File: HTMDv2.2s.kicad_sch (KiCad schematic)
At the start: 94 parts, among them IC1 TJA1441AT_0Z, IC2 A3921KLPTR-T, IC3 TMP275AQDGKRQ1, J1 Conn_01x04, J10 Conn_01x02, J11 Conn_01x02, J2 Conn_01x04, J3 Conn_01x06, J4 Conn_01x01, J5 Conn_01x01_Pin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

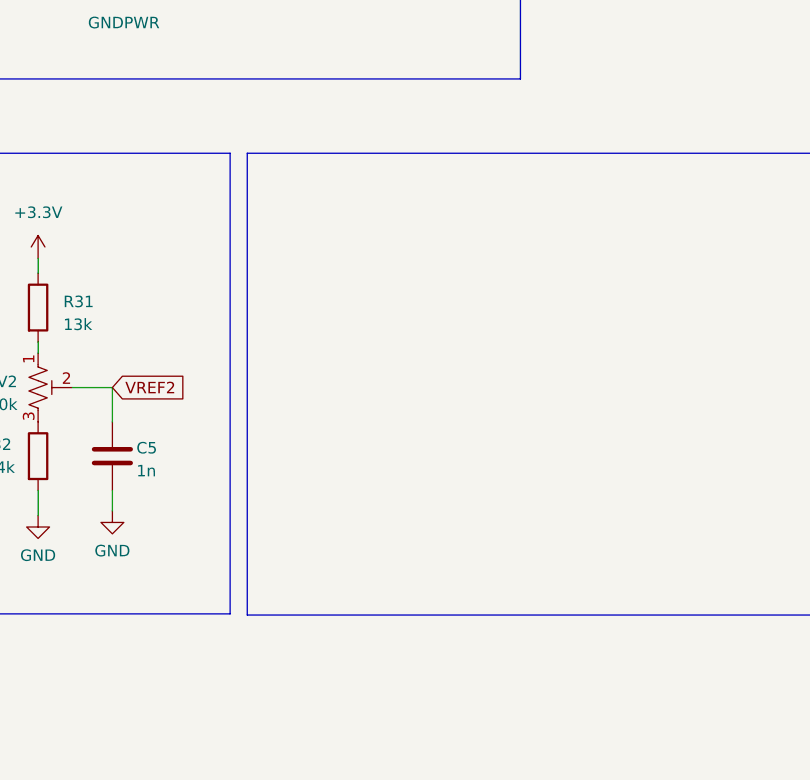
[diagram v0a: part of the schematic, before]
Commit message: Update HTMDv2.2s.kicad_sch
add LEDs
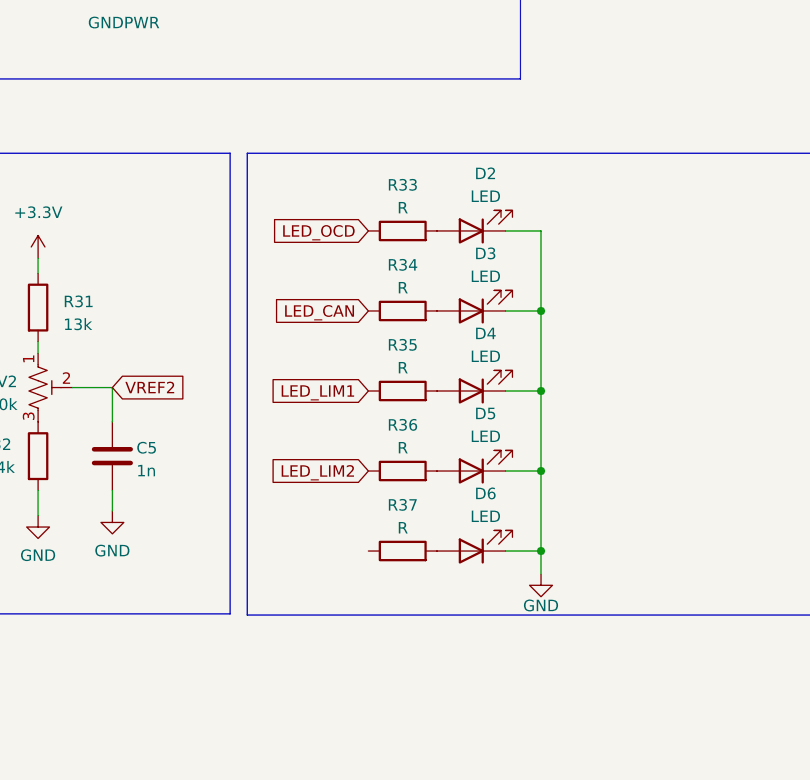
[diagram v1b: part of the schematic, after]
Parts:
- added D2, D3, D4, D5, D6: LED, LED_SMD:LED_0603_1608Metric_Pad1.05x0.95mm_HandSolder, symbol Device:LED
- added R33, R34, R35, R36, R37: R, Resistor_SMD:R_0603_1608Metric_Pad0.98x0.95mm_HandSolder, symbol Device:R
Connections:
- net GND: now also D2.1 (K), D3.1 (K), D4.1 (K), D5.1 (K), D6.1 (K)
- net LED_CAN: now also R34.1
- net LED_LIM1: now also R35.1
- net LED_LIM2: now also R36.1
- net LED_OCD: now also R33.1
- new net: D4.2 (A), R35.2
- new net: D3.2 (A), R34.2
- new net: D5.2 (A), R36.2
- new net: D6.2 (A), R37.2
- new net: D2.2 (A), R33.2

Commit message: update
change footprints
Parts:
- C7: footprint Capacitor_SMD:C_0402_1005Metric_Pad0.74x0.62mm_HandSolder -> Capacitor_SMD:C_0603_1608Metric_Pad1.08x0.95mm_HandSolder
- J6: footprint Connector_PinHeader_2.54mm:PinHeader_1x02_P2.54mm_Horizontal -> TestPoint:TestPoint_2Pads_Pitch2.54mm_Drill0.8mm
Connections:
- net SWCLK: now also J9.1 (Pin_1); no longer J9.3 (Pin_3)
- net SWDIO: now also J9.3 (Pin_3); no longer J9.1 (Pin_1)
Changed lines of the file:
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@@
     )
   )
-  (global_label "SWCLK" (shape input) (at 381 40.259 0) (fields_autoplaced)
-    (effects (font (size 1.27 1.27)) (justify left))
-    (property "Intersheetrefs" "${INTERSHEET_REFS}" (at 390.2142 40.259 0)
+  (global_label "SWCLK" (shape input) (at 381 45.339 0) (fields_autoplaced)
+    (effects (font (size 1.27 1.27)) (justify left))
+    (property "Intersheetrefs" "${INTERSHEET_REFS}" (at 390.2142 45.339 0)
       (effects (font (size 1.27 1.27)) (justify left) hide)
     )
@@
     )
   )
-  (global_label "SWDIO" (shape input) (at 381 45.339 0) (fields_autoplaced)
-    (effects (font (size 1.27 1.27)) (justify left))
-    (property "Intersheetrefs" "${INTERSHEET_REFS}" (at 389.8514 45.339 0)
+  (global_label "SWDIO" (shape input) (at 381 40.259 0) (fields_autoplaced)
+    (effects (font (size 1.27 1.27)) (justify left))
+    (property "Intersheetrefs" "${INTERSHEET_REFS}" (at 389.8514 40.259 0)
       (effects (font (size 1.27 1.27)) (justify left) hide)
     )
@@
       (effects (font (size 1.27 1.27)))
     )
-    (property "Footprint" "Capacitor_SMD:C_0402_1005Metric_Pad0.74x0.62mm_HandSolder" (at 216.027 240.0808 0)
+    (property "Footprint" "Capacitor_SMD:C_0603_1608Metric_Pad1.08x0.95mm_HandSolder" (at 216.027 240.0808 0)
       (effects (font (size 1.27 1.27)) hide)
     )
@@
       (effects (font (size 1.27 1.27)))
     )
-    (property "Footprint" "Connector_PinHeader_2.54mm:PinHeader_1x02_P2.54mm_Horizontal" (at 365.633 62.103 0)
-      (effects (font (size 1.27 1.27)) hide)
-    )
+    (property "Footprint" "TestPoint:TestPoint_2Pads_Pitch2.54mm_Drill0.8mm" (at 365.633 62.103 0)
+      (effects (font (size 1.27 1.27)) hide)
+    )

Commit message: update
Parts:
- added R38: 20k, Resistor_SMD:R_0603_1608Metric_Pad0.98x0.95mm_HandSolder, symbol Device:R
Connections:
- net GND: now also R38.2; no longer U2.46 (PB8)
- new net: R38.1, U2.46 (PB8)
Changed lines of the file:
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@@
     (stroke (width 0) (type default))
   )
-  (wire (pts (xy 64.389 199.263) (xy 64.389 180.975))
+  (wire (pts (xy 64.389 199.263) (xy 64.389 195.072))
     (stroke (width 0) (type default))
   )
@@
     (stroke (width 0) (type default))
   )
+  (wire (pts (xy 64.389 187.452) (xy 64.389 180.975))
+    (stroke (width 0) (type default))
+  )
   (wire (pts (xy 235.458 108.204) (xy 261.62 108.204))
     (stroke (width 0) (type default))
@@
         )
       )
+    )
+  )
+  (symbol (lib_id "Device:R") (at 64.389 191.262 0) (unit 1)
+    (in_bom yes) (on_board yes) (dnp no) (fields_autoplaced)
+    (property "Reference" "R38" (at 66.548 190.627 0)
+      (effects (font (size 1.27 1.27)) (justify left))
+    )
+    (property "Value" "20k" (at 66.548 193.167 0)
+      (effects (font (size 1.27 1.27)) (justify left))
+    )
+    (property "Footprint" "Resistor_SMD:R_0603_1608Metric_Pad0.98x0.95mm_HandSolder" (at 62.611 191.262 90)
+      (effects (font (size 1.27 1.27)) hide)
+    )
+    (property "Datasheet" "~" (at 64.389 191.262 0)
+      (effects (font (size 1.27 1.27)) hide)
+    )
+    (pin "1")
+    (pin "2")
+    (instances
+      (project "HTMDv2.2s"
+        (path "/b4476ce1-4dbe-4b8d-acdf-5a8a6cb2187e"
+          (reference "R38") (unit 1)
+        )
+      )

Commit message: update
add power line
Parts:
- removed D1: D, 0-Myparts:SS2040FL, symbol Device:D
- removed U1: ADP3338AKCZ-3.3, 0-Myparts:SOT230P700X180-4N, symbol 0-Myparts:ADP3338AKCZ-3.3
- added C24: 4.7u, symbol Device:C
- added C25: C, Capacitor_SMD:C_0603_1608Metric_Pad1.08x0.95mm_HandSolder, symbol Device:C
- added C28, C29: 10u, Capacitor_SMD:C_0805_2012Metric_Pad1.18x1.45mm_HandSolder, symbol Device:C
- added L1: 4.7u, Inductor_SMD:L_0603_1608Metric_Pad1.05x0.95mm_HandSolder, symbol Device:L
- added R39, R40: R, Resistor_SMD:R_0603_1608Metric_Pad0.98x0.95mm_HandSolder, symbol Device:R
- added R41: 100k, symbol Device:R
- added U1: TPS628511DRLR, 0_Mylib:DRL0008A-MFG, symbol 0_symbols:TPS628511DRLR
- C2, C3: value 1u -> 10u; footprint Capacitor_SMD:C_0603_1608Metric_Pad1.08x0.95mm_HandSolder -> Capacitor_SMD:C_0805_2012Metric_Pad1.18x1.45mm_HandSolder
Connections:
- net +3.3V: now also C25.1, C28.1, C29.1, L1.2, R39.1, R41.1; no longer C3.1
- net GND: now also C24.2, C28.2, C29.2, R40.2, U1.8 (GND)
- net VCC: now also C3.1, U1.1 (VIN), U1.2 (EN), U1.3 (MODE_SYNC)
- new net: C24.1, U1.4 (SS_TR)
- new net: C25.2, R39.2, R40.1, U1.5 (FB)
- new net: L1.1, U1.7 (SW)
- new net: R41.2, U1.6 (PG)

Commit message: update
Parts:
- C24: footprint (none) -> Capacitor_SMD:C_0603_1608Metric_Pad1.08x0.95mm_HandSolder
- J9: footprint Connector_PinHeader_2.54mm:PinHeader_1x04_P2.54mm_Horizontal -> Connector_PinHeader_2.54mm:PinHeader_1x04_P2.54mm_Vertical
- R41: footprint (none) -> Inductor_SMD:L_0603_1608Metric_Pad1.05x0.95mm_HandSolder
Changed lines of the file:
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@@
       (effects (font (size 1.27 1.27)) (justify left))
     )
-    (property "Footprint" "" (at 90.3732 60.706 0)
+    (property "Footprint" "Capacitor_SMD:C_0603_1608Metric_Pad1.08x0.95mm_HandSolder" (at 90.3732 60.706 0)
       (effects (font (size 1.27 1.27)) hide)
     )
@@
       (effects (font (size 1.27 1.27)) (justify left))
     )
-    (property "Footprint" "" (at 153.162 41.91 90)
+    (property "Footprint" "Inductor_SMD:L_0603_1608Metric_Pad1.05x0.95mm_HandSolder" (at 153.162 41.91 90)
       (effects (font (size 1.27 1.27)) hide)
     )
@@
       (effects (font (size 1.27 1.27)))
     )
-    (property "Footprint" "Connector_PinHeader_2.54mm:PinHeader_1x04_P2.54mm_Horizontal" (at 363.728 42.799 0)
-      (effects (font (size 1.27 1.27)) hide)
+    (property "Footprint" "Connector_PinHeader_2.54mm:PinHeader_1x04_P2.54mm_Vertical" (at 363.728 42.799 0)
+      (effects (font (size 1.27 1.27)))
     )
     (property "Datasheet" "~" (at 363.728 42.799 0)

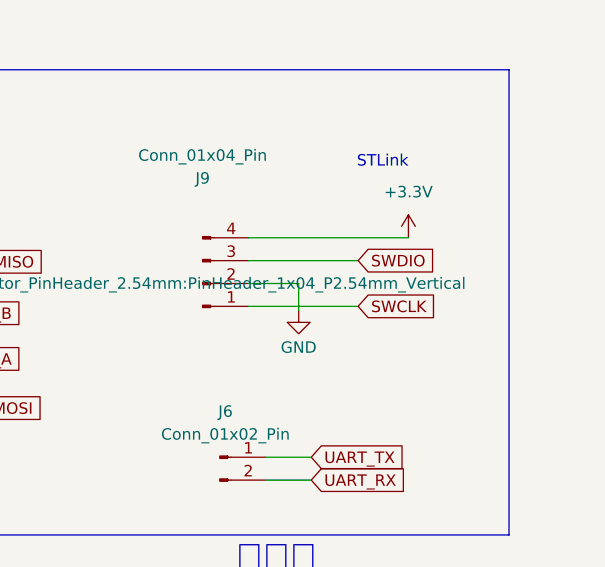
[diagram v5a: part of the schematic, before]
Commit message: update
SYS配線の見直し
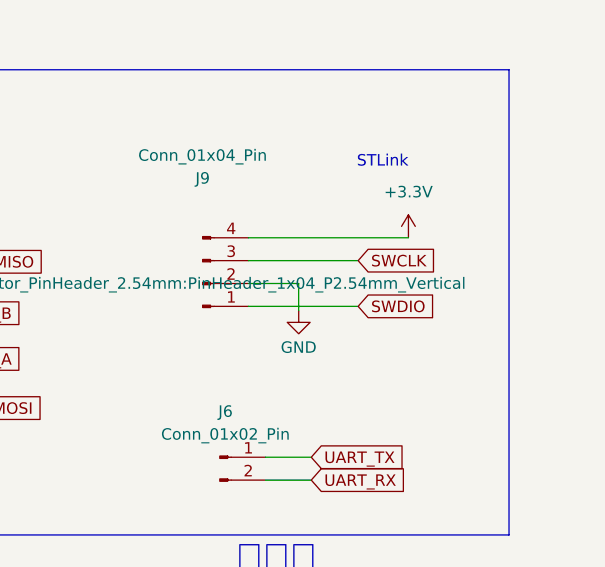
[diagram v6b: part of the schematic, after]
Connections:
- net SWCLK: now also J9.3 (Pin_3); no longer J9.1 (Pin_1)
- net SWDIO: now also J9.1 (Pin_1); no longer J9.3 (Pin_3)
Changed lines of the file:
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@@
     )
   )
-  (global_label "SWCLK" (shape input) (at 381 45.339 0) (fields_autoplaced)
+  (global_label "SWCLK" (shape input) (at 381 40.259 0) (fields_autoplaced)
     (effects (font (size 1.27 1.27)) (justify left))
-    (property "Intersheetrefs" "${INTERSHEET_REFS}" (at 390.2142 45.339 0)
+    (property "Intersheetrefs" "${INTERSHEET_REFS}" (at 390.2142 40.259 0)
       (effects (font (size 1.27 1.27)) (justify left) hide)
     )
@@
     )
   )
-  (global_label "SWDIO" (shape input) (at 381 40.259 0) (fields_autoplaced)
+  (global_label "SWDIO" (shape input) (at 381 45.339 0) (fields_autoplaced)
     (effects (font (size 1.27 1.27)) (justify left))
-    (property "Intersheetrefs" "${INTERSHEET_REFS}" (at 389.8514 40.259 0)
+    (property "Intersheetrefs" "${INTERSHEET_REFS}" (at 389.8514 45.339 0)
       (effects (font (size 1.27 1.27)) (justify left) hide)
     )

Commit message: pre cmpl
レビューまち
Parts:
- added D1, D7, D8, D9: LED, LED_SMD:LED_0603_1608Metric_Pad1.05x0.95mm_HandSolder, symbol Device:LED
- added R42, R43, R44, R45: R, Resistor_SMD:R_0603_1608Metric_Pad0.98x0.95mm_HandSolder, symbol Device:R
- JP2, JP3, JP4, JP5: footprint Jumper:SolderJumper-2_P1.3mm_Open_TrianglePad1.0x1.5mm -> Resistor_SMD:R_0603_1608Metric_Pad0.98x0.95mm_HandSolder
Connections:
- net ENC_B: now also JP5.2 (B); no longer JP2.2 (B)
- net GND: now also D1.1 (K), D7.1 (K), D8.1 (K), D9.1 (K)
- net LED1: now also R37.1, U2.24 (PB11); no longer U2.29 (PC6)
- net LED2: now also U2.19 (PB2), R42.1; no longer U2.28 (PB15)
- net LED3: now also U2.18 (PB1), R43.1; no longer U2.27 (PB14)
- net LED4: now also U2.17 (PB0), R44.1; no longer U2.26 (PB13)
- net LED5: now also U2.13 (PA5), R45.1; no longer U2.25 (PB12)
- net SPI_CS: now also U2.25 (PB12); no longer U2.16 (PC4)
- net SPI_MISO: now also U2.27 (PB14); no longer U2.14 (PA6)
- net SPI_MOSI: now also JP2.2 (B), U2.28 (PB15); no longer JP5.2 (B), U2.15 (PA7)
- net SPI_SCK: now also U2.26 (PB13); no longer U2.13 (PA5)
- net at J3.3 (Pin_3), JP3.1 (A): now also JP5.1 (A); no longer JP2.1 (A)
- net at J3.1 (Pin_1), JP4.1 (A): now also JP2.1 (A); no longer JP5.1 (A)
- new net: D1.2 (A), R42.2
- new net: D9.2 (A), R45.2
- new net: D8.2 (A), R44.2
- new net: D7.2 (A), R43.2

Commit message: update
温度センサ周りの配線
プルダウン抵抗の位置変更
ドライブラインのLED追加
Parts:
- added C30: 0.1u, Capacitor_SMD:C_0603_1608Metric_Pad1.08x0.95mm_HandSolder, symbol Device:C
- added C31: 1u, Capacitor_SMD:C_0603_1608Metric_Pad1.08x0.95mm_HandSolder, symbol Device:C
- added D10, D11: D, 0-Myparts:SS2040FL, symbol Device:D
- added D12, D13, D14, D15, D16, D17, D18: LED, LED_SMD:LED_0603_1608Metric_Pad1.05x0.95mm_HandSolder, symbol Device:LED
- added R46, R47, R48, R49, R50, R51, R52: R, Resistor_SMD:R_0603_1608Metric_Pad0.98x0.95mm_HandSolder, symbol Device:R
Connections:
- net +24V: now also R48.1
- net +3.3V: now also C30.1, C31.1, D11.2 (A), R46.1
- net GND: now also C30.2, C31.2, D12.1 (K), D13.1 (K), D15.1 (K), D16.1 (K), D17.1 (K), D18.1 (K)
- net GNDPWR: now also D14.1 (K)
- net OPHASE1: now also R52.1
- net OPWMH1: now also R49.1
- net OPWML1: now also R50.1
- net OSR1: now also R51.1
- net VCC: now also D10.2 (A), D11.1 (K), R47.1; no longer C2.1, C3.1, U1.1 (VIN), U1.2 (EN), U1.3 (MODE_SYNC)
- new net: D17.2 (A), R51.2
- new net: D12.2 (A), R46.2
- new net: D18.2 (A), R52.2
- new net: C2.1, C3.1, D10.1 (K), U1.1 (VIN), U1.2 (EN), U1.3 (MODE_SYNC)
- new net: D13.2 (A), R47.2
- new net: D16.2 (A), R50.2
- new net: D15.2 (A), R49.2
- new net: D14.2 (A), R48.2
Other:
- moved on the sheet: C1, C10, C11, C12, C2, C24, C25, C28, C29, C3, D1, D2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
